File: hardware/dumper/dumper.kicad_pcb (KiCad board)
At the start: 2 copper layers, 103.5 x 61 mm, 19 parts, among them J1 /Reset, J2 Clock In, J3 unknown, J4 unknown 2, J5 2816 /WR disconnect, U1 4011, U2 DS1225Y-150, U3 74HC373, U4 PIC70x2

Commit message: finished initial layout
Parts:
- added J10: arduino 10, Connector_PinHeader_2.54mm:PinHeader_1x01_P2.54mm_Vertical, F.Cu at (97.2, 116.8)
- added J11: ss, Connector_PinHeader_2.54mm:PinHeader_1x01_P2.54mm_Vertical, F.Cu at (99.7, 116.8)
- added J6: arduino 13, Connector_PinHeader_2.54mm:PinHeader_1x01_P2.54mm_Vertical, F.Cu at (97.2, 112.4)
- added J7: arduino 11, Connector_PinHeader_2.54mm:PinHeader_1x01_P2.54mm_Vertical, F.Cu at (97.2, 108.0)
- added J8: arduino 5, Connector_PinHeader_2.54mm:PinHeader_1x01_P2.54mm_Vertical, F.Cu at (98.4, 139.1)
- added J9: arduino 7, Connector_PinHeader_2.54mm:PinHeader_1x01_P2.54mm_Vertical, F.Cu at (98.4, 131.4)
- J3: value unknown -> data
- J4: value unknown 2 -> clock
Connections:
- A1 pad 10: unconnected-(A1-Pad10) -> /RESET
- A1 pad 13: unconnected-(A1-Pad13) -> B3
- A1 pad 14: unconnected-(A1-Pad14) -> B1
- A1 pad 16: unconnected-(A1-Pad16) -> B2
- A1 pad 8: unconnected-(A1-Pad8) -> XTAL2
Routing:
- net B3: track 0.00 -> 45.0 mm, vias 0 -> 2
- net B2: track 6.02 -> 34.5 mm
- net /INT1: track 173.3 -> 200.9 mm
- net XTAL2: track 3.81 -> 27.3 mm
- net /RESET: track 3.81 -> 24.7 mm
- net B1: track 5.23 -> 14.9 mm
- net C1: track 54.8 -> 54.1 mm

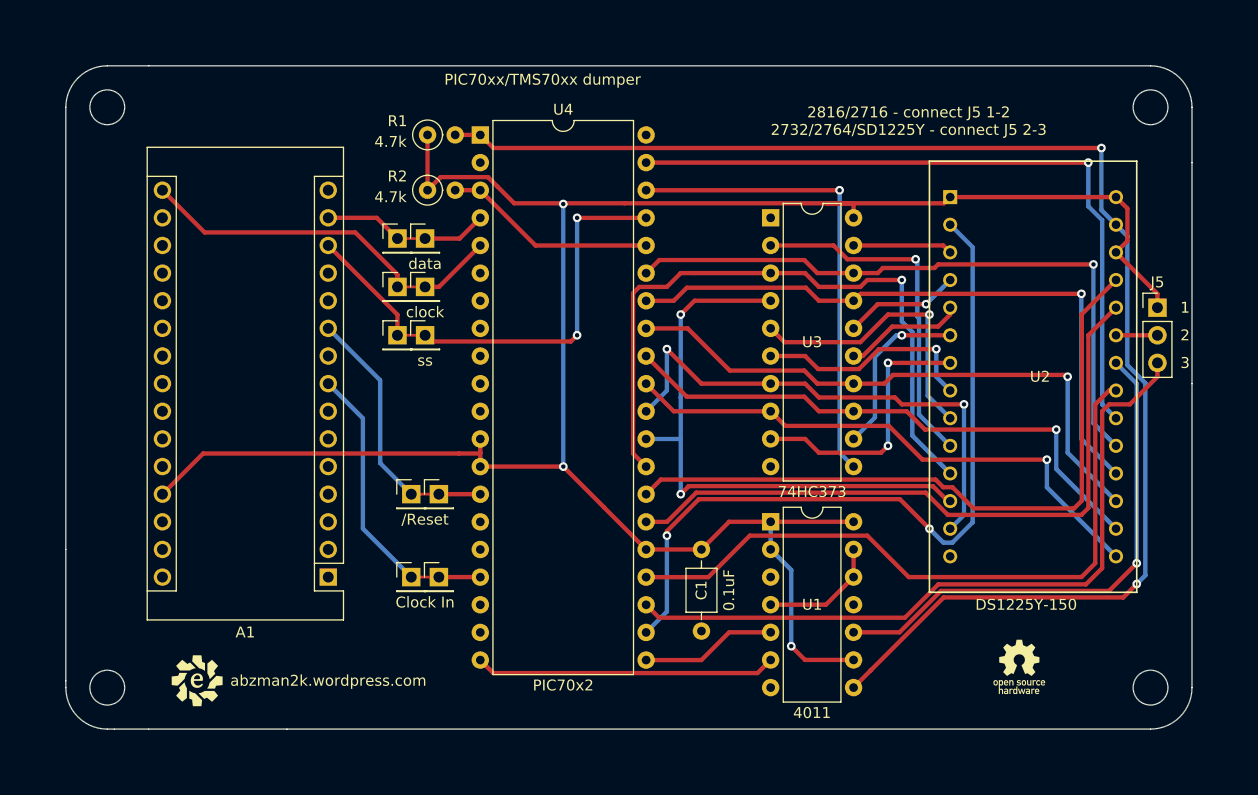
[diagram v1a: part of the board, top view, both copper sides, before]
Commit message: Simplified the schematic - no external writes needed
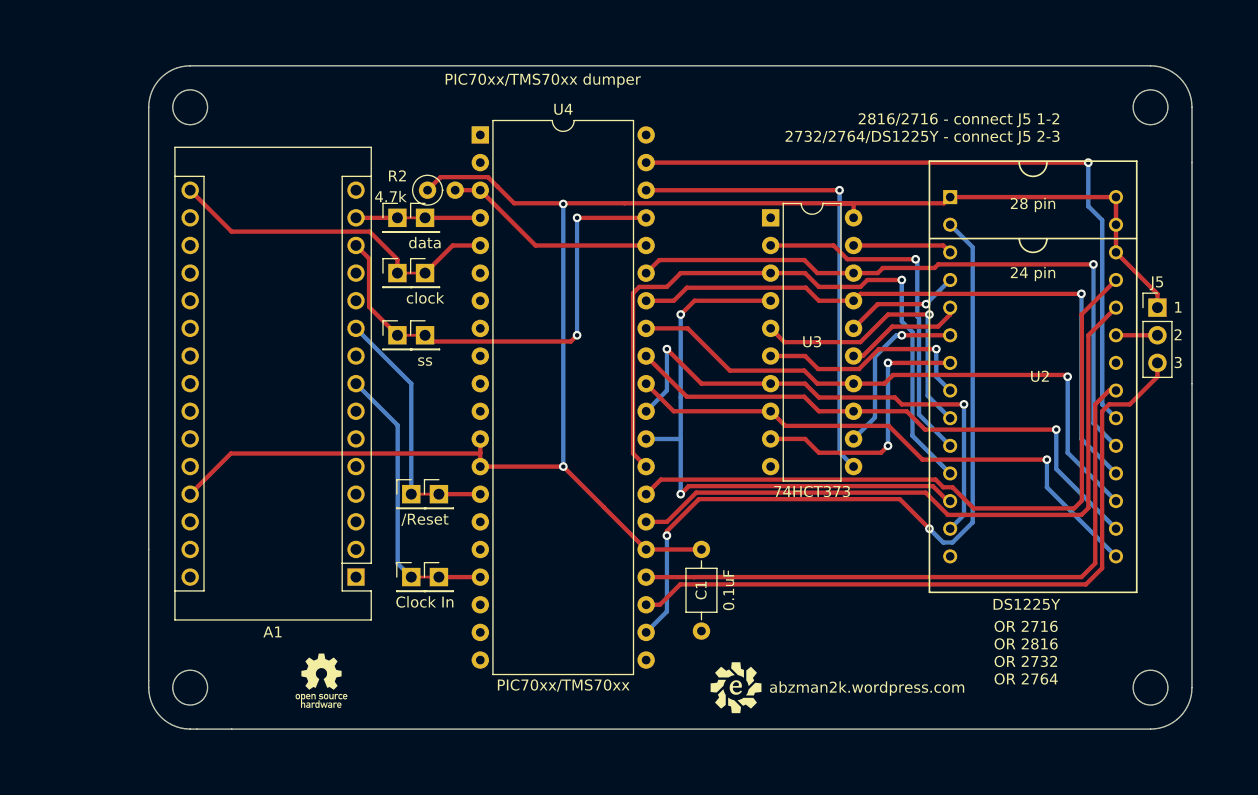
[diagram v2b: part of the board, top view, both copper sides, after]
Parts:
- removed R1: 4.7k, Resistor_THT:R_Axial_DIN0207_L6.3mm_D2.5mm_P2.54mm_Vertical
- removed U1: 4011, Package_DIP:DIP-14_W7.62mm
- U2: value DS1225Y-150 -> DS1225Y
- U3: value 74HC373 -> 74HCT373
- U4: value PIC70x2 -> PIC70xx/TMS70xx
- moved G*** 64.1 mm to (90.2, 148.6)
- moved G*** 49.5 mm to (128.3, 149.2)
- moved REF** 7.62 mm to (78.1, 95.9)
- moved REF** 7.62 mm to (78.1, 149.2)
- moved A1 2.55 mm to (93.3, 139.1)
- moved J3 1.91 mm to (99.7, 106.0)
- moved J7 1.91 mm to (97.2, 106.0)
- moved J4 1.27 mm to (99.7, 111.1)
- moved J6 1.27 mm to (97.2, 111.1)
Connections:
- U2 pad 22: Net-(U1-Pad10) -> GND
- U2 pad 27: B5 -> /INT1
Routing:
- net B5: track 131.9 -> 0.00 mm, vias 2 -> 0
- net Net-(U1-Pad10): track 47.9 -> 0.00 mm, vias 1 -> 0
- net /INT1: track 200.9 -> 158.9 mm, vias 3 -> 2
- net D6: track 27.7 -> 0.00 mm
- net D5: track 12.5 -> 0.00 mm
- net Net-(U1-Pad12): track 11.2 -> 0.00 mm
- net B1: track 14.9 -> 11.4 mm
- net D2: track 62.0 -> 58.8 mm
- net B2: track 34.5 -> 31.7 mm
- net /RESET: track 24.7 -> 23.7 mm
- net B3: track 45.0 -> 44.0 mm
- net XTAL2: track 27.3 -> 26.2 mm
- net D3: track 66.4 -> 65.4 mm
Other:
- board size 103.5 x 61 mm -> 95.9 x 61 mm
- board text added: "24 pin"
- board text added: "28 pin"
- board text added: "2816/2716 - connect J5 1-2 2732/2764/DS1225Y - connect J5 2-3"
- board text added: "Code loaded into the EPROM/NVRAM runs and dumps the code to the Arduino."
- board text added: "OR 2716 OR 2816 OR 2732 OR 2764"
- board text removed: "2816/2716 - connect J5 1-2 2732/2764/SD1225Y - connect J5 2-3"
- board text removed: "Code loaded into the EPROM/NVRAM runs and dumps the code to the arduino. Optionally the microcontroller has control of the write line to the NVRAM This lets the microcontroller write its own code into the NVRAM while it is just clocked"

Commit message: updated board layout
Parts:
- moved R2 22.7 mm to (122.6, 104.8), turned to -90 degrees
- moved G*** 7.10 mm to (96.5, 145.4)
- moved G*** 6.84 mm to (130.8, 142.9)
- moved REF** 6.26 mm to (160.6, 146.7)
- moved REF** 6.26 mm to (160.6, 98.4)
- moved U3 5.73 mm to (125.7, 106.0)
- moved J5 5.72 mm to (161.3, 114.3)
- moved U2 5.72 mm to (157.5, 137.2)
- moved REF** 2.54 mm to (78.1, 98.4)
- moved REF** 2.54 mm to (78.1, 146.7)
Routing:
- net /INT1: track 158.9 -> 137.5 mm
- net C1: track 54.1 -> 42.7 mm
- net B6: track 65.2 -> 58.3 mm
- net D1: track 62.3 -> 56.6 mm
- net C6: track 59.1 -> 53.4 mm
- net C0: track 62.3 -> 56.6 mm
- net D2: track 58.8 -> 53.1 mm
- net C5: track 54.5 -> 48.8 mm
- net C7: track 60.0 -> 54.2 mm
- net C4: track 51.9 -> 46.2 mm
- net C3: track 51.2 -> 45.5 mm
- net B4: track 43.7 -> 38.0 mm
- net D3: track 65.4 -> 59.7 mm
- net D4: track 70.1 -> 64.3 mm
- net C2: track 47.9 -> 42.2 mm
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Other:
- board size 95.9 x 61 mm -> 90.2 x 55.9 mm
- board text added: "5v"
- board text added: "d10"
- board text added: "d11"
- board text added: "d13"
- board text added: "d5"
- board text added: "d7"
- board text added: "gnd"
- board text added: "usb side"

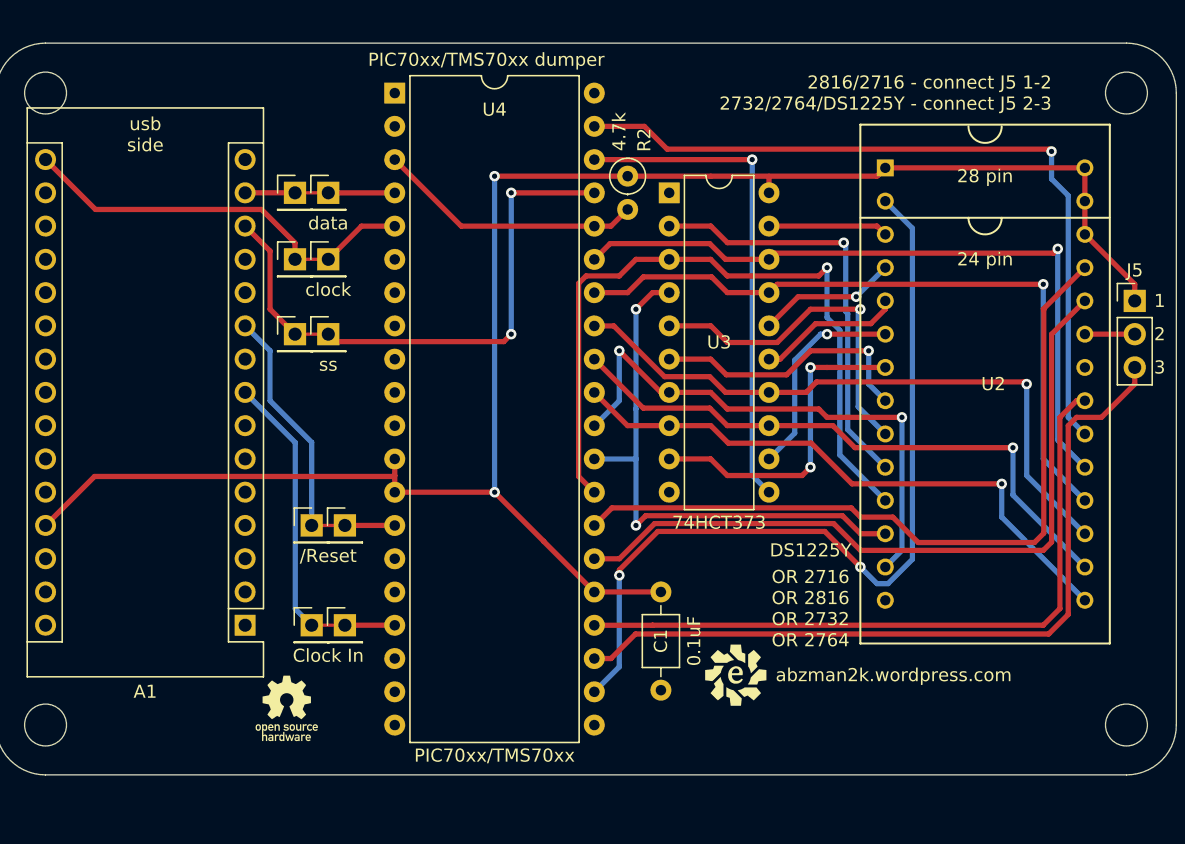
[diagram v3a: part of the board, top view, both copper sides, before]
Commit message: added button and LED, still need software support though
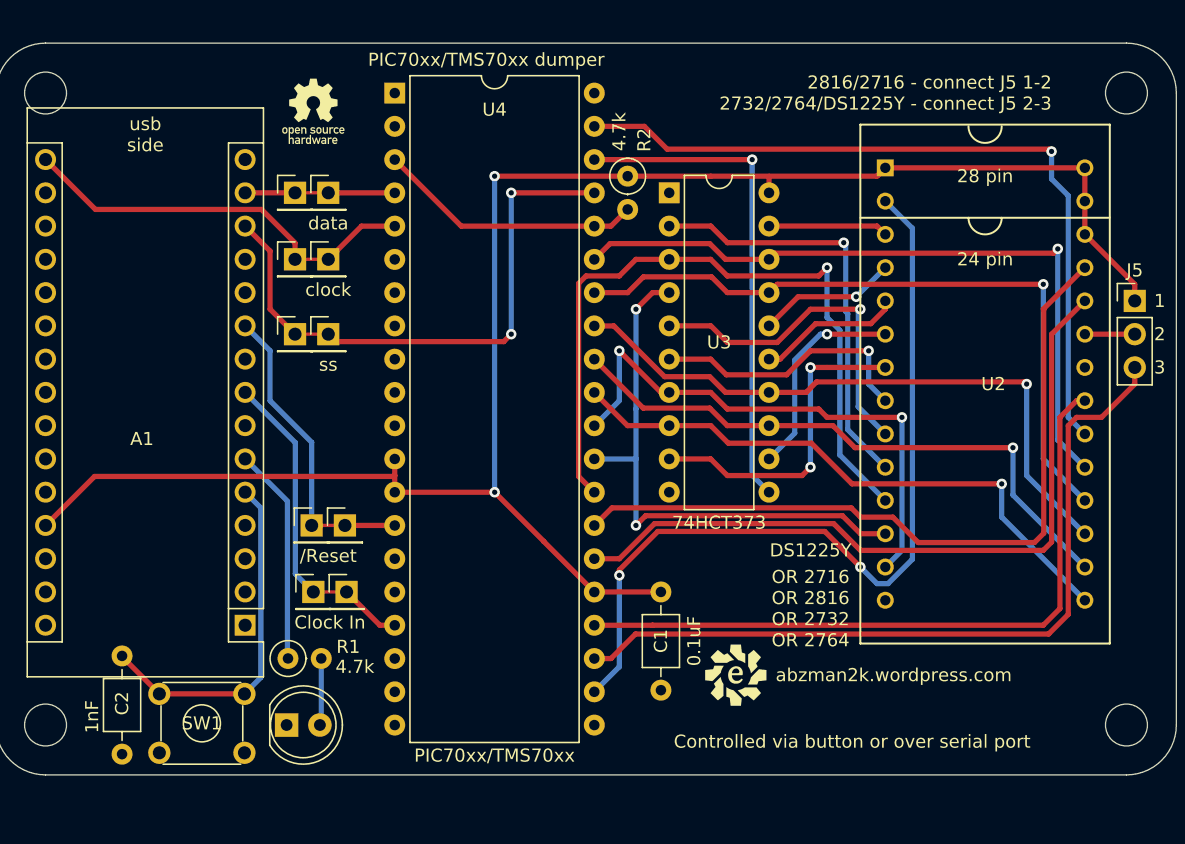
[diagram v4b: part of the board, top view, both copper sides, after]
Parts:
- added C2: 1nF, Capacitor_THT:C_Axial_L3.8mm_D2.6mm_P7.50mm_Horizontal, F.Cu at (83.9, 148.9)
- added D1: LED, LED_THT:LED_D5.0mm, F.Cu at (96.5, 146.7)
- added R1: 4.7k, Resistor_THT:R_Axial_DIN0207_L6.3mm_D2.5mm_P2.54mm_Vertical, F.Cu at (96.6, 141.6)
- added SW1: SW_MEC_5E, Button_Switch_THT:SW_TH_Tactile_Omron_B3F-10xx, F.Cu at (93.3, 148.8)
- moved G*** 45.6 mm to (98.6, 99.8)
- moved J8 2.54 mm to (98.6, 136.5)
- moved J2 2.54 mm to (101.1, 136.5)
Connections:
- A1 pad 5: unconnected-(A1-Pad5) -> Net-(A1-Pad5)
- A1 pad 6: unconnected-(A1-Pad6) -> Net-(A1-Pad6)
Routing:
- net Net-(A1-Pad5): track 0.00 -> 27.0 mm
- net Net-(A1-Pad6): track 0.00 -> 16.6 mm
- net Net-(D1-Pad2): track 0.00 -> 5.12 mm
- net XTAL2: track 26.2 -> 24.7 mm
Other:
- board text added: "Controlled via button or over serial port"

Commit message: added gerbers
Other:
- board text added: "Code loaded into the EPROM/NVRAM runs and dumps the internal code of the PIC7000 to the Arduino."
- board text added: "d2"
- board text added: "d3"
- board text removed: "Code loaded into the EPROM/NVRAM runs and dumps the code to the Arduino."
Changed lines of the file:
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@@
       (layerselection 0x00010fc_ffffffff)
       (disableapertmacros false)
-      (usegerberextensions false)
+      (usegerberextensions true)
       (usegerberattributes true)
       (usegerberadvancedattributes true)
-      (creategerberjobfile true)
+      (creategerberjobfile false)
       (svguseinch false)
       (svgprecision 6)
@@
       (plotinvisibletext false)
       (sketchpadsonfab false)
-      (subtractmaskfromsilk false)
+      (subtractmaskfromsilk true)
       (outputformat 1)
       (mirror false)
-      (drillshape 1)
+      (drillshape 0)
       (scaleselection 1)
-      (outputdirectory "")
+      (outputdirectory "pic7000 dumper gerbers/")
     )
   )
@@
     (effects (font (size 1 1) (thickness 0.15)) (justify mirror))
   )
+  (gr_text "d3" (at 91.44 126.492) (layer "B.SilkS")
+    (effects (font (size 1 1) (thickness 0.15)) (justify mirror))
+  )
   (gr_text "d10" (at 90.805 108.585) (layer "B.SilkS")
     (effects (font (size 1 1) (thickness 0.15)) (justify mirror))
@@
     (effects (font (size 1 1) (thickness 0.15)) (justify mirror))
   )
+  (gr_text "d2" (at 91.44 128.778) (layer "B.SilkS")
+    (effects (font (size 1 1) (thickness 0.15)) (justify mirror))
+  )
   (gr_text "d7" (at 91.44 116.205) (layer "B.SilkS")
     (effects (font (size 1 1) (thickness 0.15)) (justify mirror))
@@
     (effects (font (size 1 1) (thickness 0.15)) (justify mirror))
   )
-  (gr_text "Code loaded into the EPROM/NVRAM runs \nand dumps the code to the Arduino." (at 147.955 123.825 90) (layer "B.SilkS")
+  (gr_text "Code loaded into the EPROM/NVRAM runs \nand dumps the internal code of the PIC7000 to the Arduino." (at 147.955 123.825 90) (layer "B.SilkS")
     (effects (font (size 1 1) (thickness 0.15)) (justify mirror))
   )
@@
   (segment (start 101.092 136.525) (end 103.637 139.07) (width 0.4) (layer "F.Cu") (net 26))
   (segment (start 98.552 136.525) (end 101.092 136.525) (width 0.25) (layer "F.Cu") (net 26))
-  (segment (start 104.765 139.065) (end 104.77 139.07) (width 0.4) (layer "F.Cu") (net 26))
   (segment (start 103.637 139.07) (end 104.77 139.07) (width 0.4) (layer "F.Cu") (net 26))
   (segment (start 97.175489 125.115489) (end 97.175489 135.148489) (width 0.4) (layer "B.Cu") (net 26))

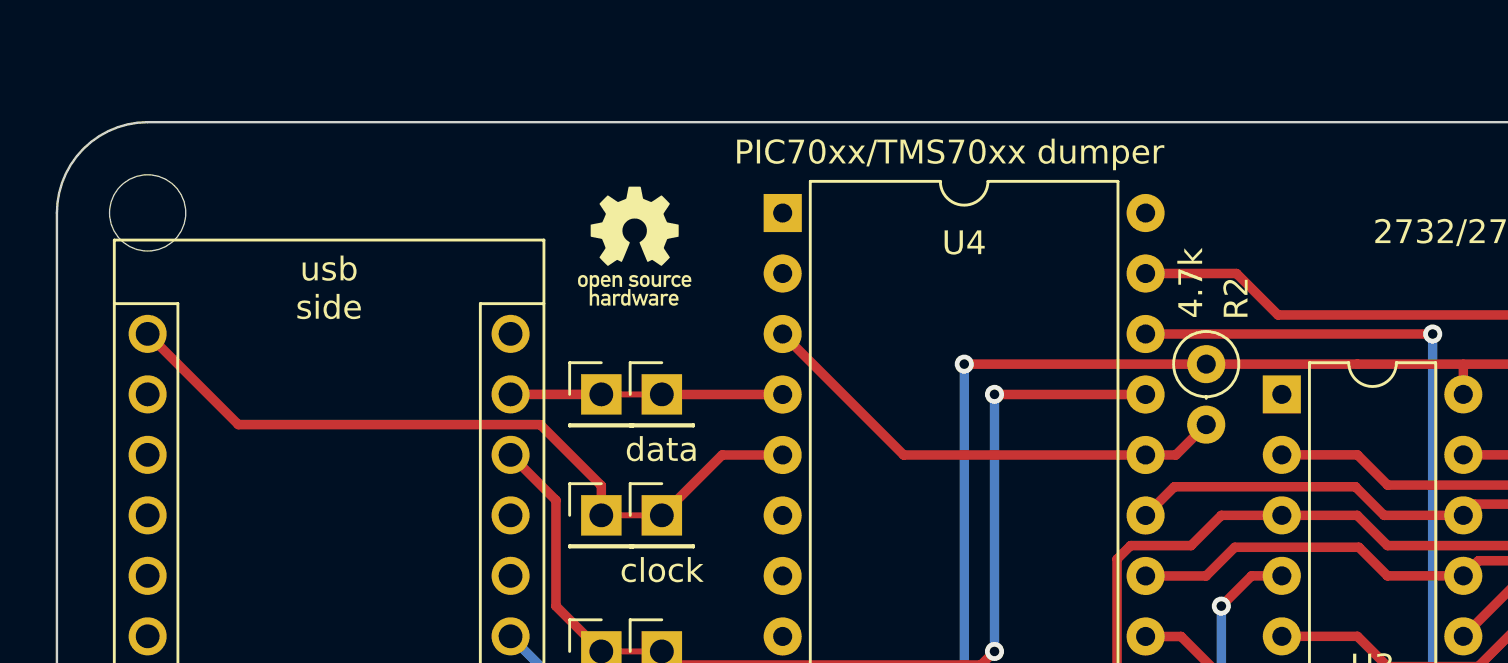
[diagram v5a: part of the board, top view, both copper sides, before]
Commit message: added version B changes
silk update and analog sense wire
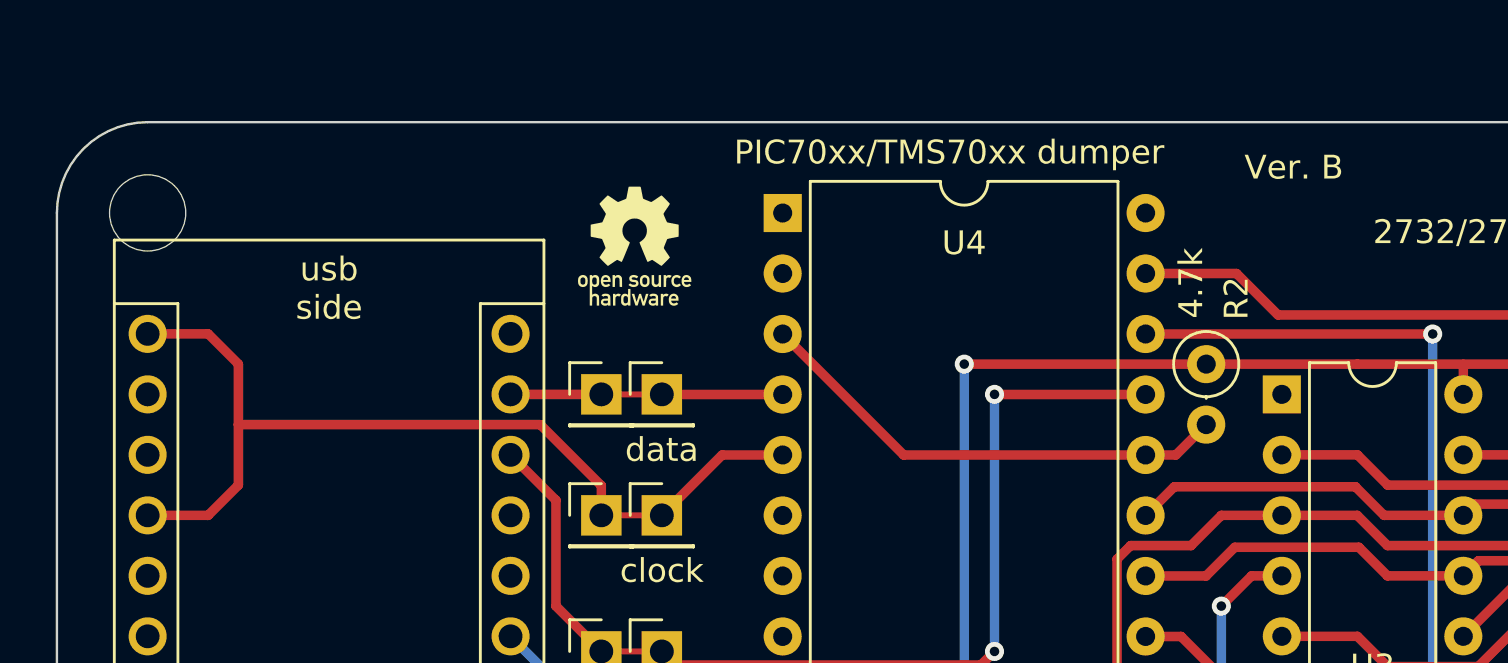
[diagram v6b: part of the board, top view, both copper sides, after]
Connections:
- A1 pad 19: unconnected-(A1-Pad19) -> B2
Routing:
- net B2: track 31.6 -> 40.0 mm
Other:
- board text added: "Ver. B"
- board text added: "a0"
